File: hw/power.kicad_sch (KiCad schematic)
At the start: 42 parts, among them J2 USB B Micro, Q1 AP2301, Q2 AP2302, Q3 AP2301, Q8 AP2301, SW1 ON/OFF, U2 AP3401KTTR, U3 MIC2250-2YD5-TR, U4 MCP73831-2ATI, U7 SE809

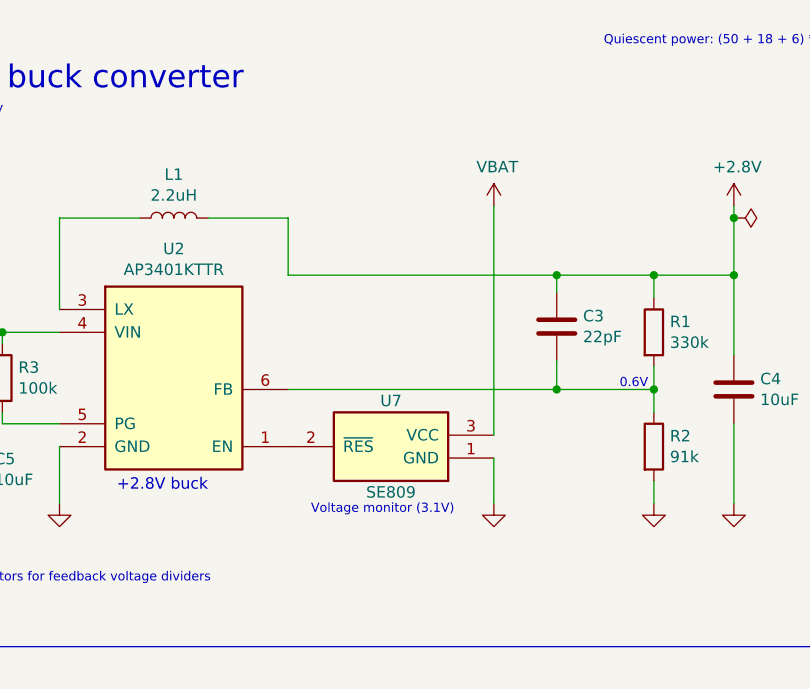
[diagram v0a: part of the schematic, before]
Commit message: PCB: removed reset monitor
Causes drop in power when USB is disconnected and not really necessary.
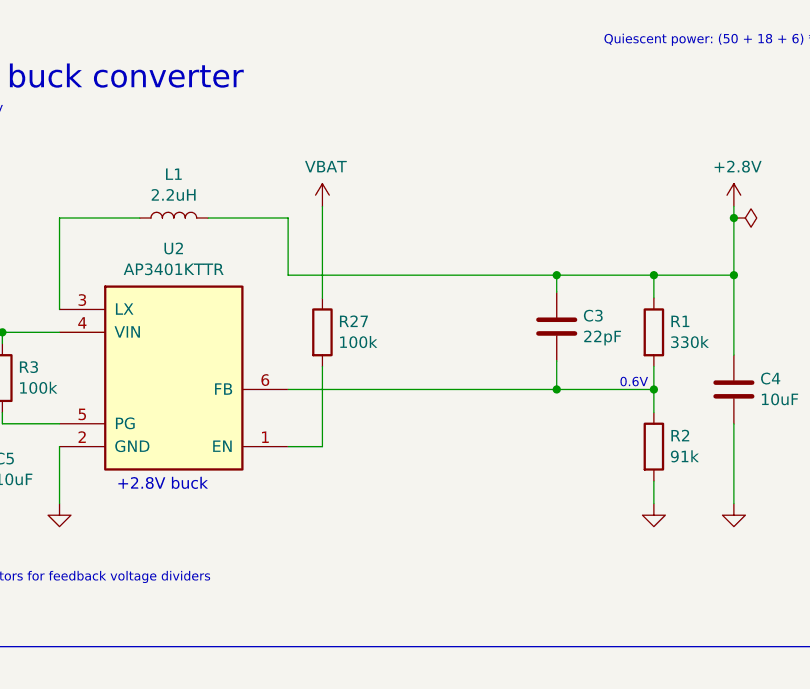
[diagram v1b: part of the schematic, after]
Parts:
- removed U7: SE809, Package_TO_SOT_SMD:SOT-23, symbol console:SE809
- added R27: 100k, Resistor_SMD:R_0603_1608Metric, symbol Device:R
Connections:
- net VBAT: now also R27.1
- net at U2.1 (EN): now also R27.2
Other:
- note removed: "Voltage monitor (3.1V)"

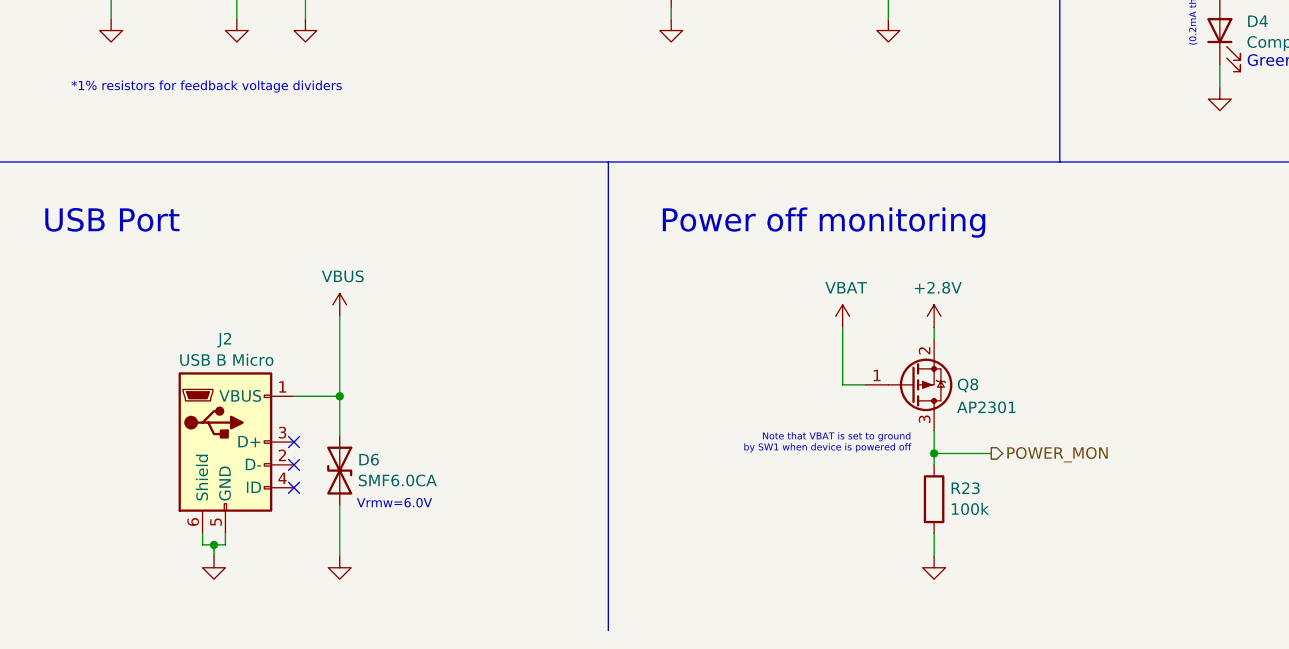
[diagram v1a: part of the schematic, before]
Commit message: PCB: removed power monitor
Far from enough capacity on board to ever be useful.
Power monitor was envisioned to prevent EEPROM corruption. This was instead prevented with atomic operation (copy before write).
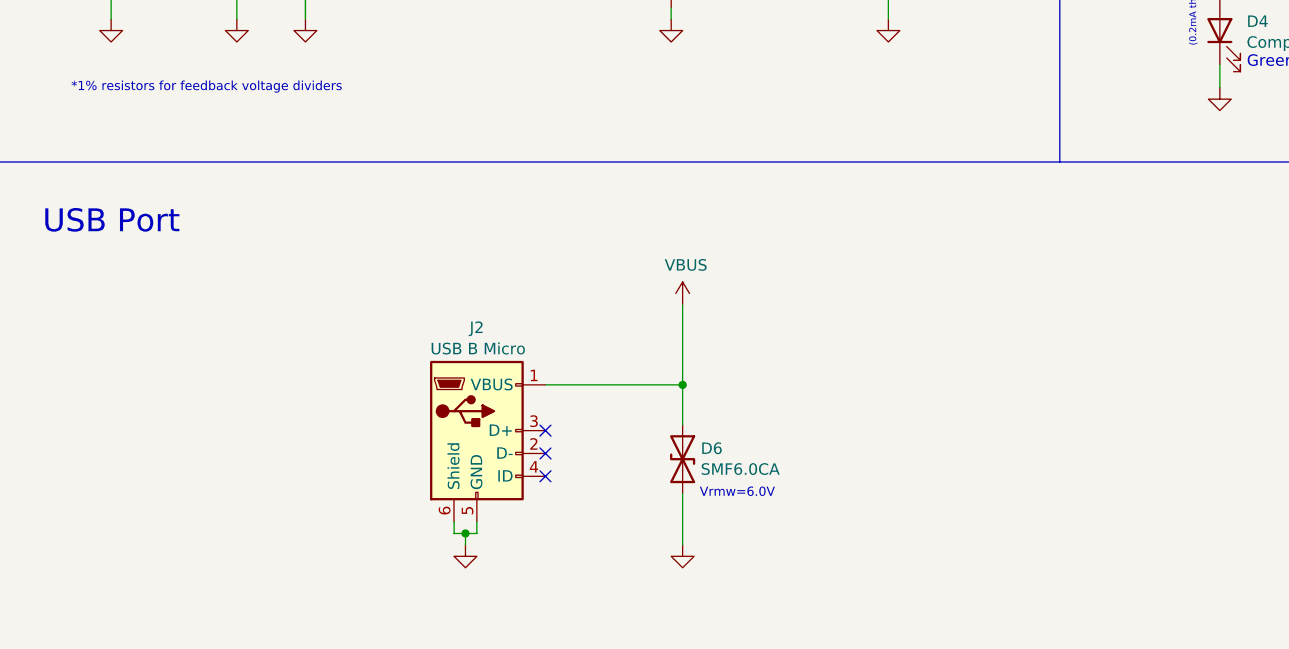
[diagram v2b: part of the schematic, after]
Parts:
- removed Q8: AP2301, Package_TO_SOT_SMD:SOT-23, symbol console:AP2301
- removed R23: 100k, Resistor_SMD:R_0603_1608Metric, symbol Device:R
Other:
- note removed: "Note that VBAT is set to ground by SW1 when device is powered off"
- note removed: "Power off monitoring"
- moved on the sheet: D6, J2
